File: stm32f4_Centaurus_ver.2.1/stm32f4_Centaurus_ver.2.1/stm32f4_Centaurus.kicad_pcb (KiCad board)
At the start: 2 copper layers, 100 x 79 mm, 215 parts, among them IC1 PIC24FJ64GB004, P1 PICKit3, P10 XA2_12V, P11 CAN0, P12 CAN1, P13 CAN0, P14 CAN1, P15 SERIAL2, P16 SERIAL0, P17 XA2_5V, P18 SWD, P2 SERIAL5_SBDBT, P23 A/D, P24 PWM, P25 A/D_batt, P26 PWM_batt, P27 EMERGENCY_CHECK, P28 I/O_5V, P29 I/O_Variable, P3 ENC0, P30 I/O_5V_batt, P31 I/O_Variable, P4 ENC2, P5 SERIAL1, P6 ENC3, P7 ENC1, P8 SERIAL4, P9 SERIAL3, Q1 FET_P, Q2 FET_P, Q3 FET_P, Q4 NPN, Q5 NPN, Q6 FET_P, Q7 FET_N, SW1 Main_POWER, SW2 SW1, SW3 SW0, SW4 SW2, SW5 SW3, U1 STM32F407VG, U10 LOGO, U12 25LC010A, U13 LOGO, U2 AZ1086H, U3 MCP2221A, U4 BD9G101G, U5 MAX3051, U6 MAX3051, U7 AQM1602_BL, U8 OSTBABS4C2B, U9 LOGO, X1 8MHz

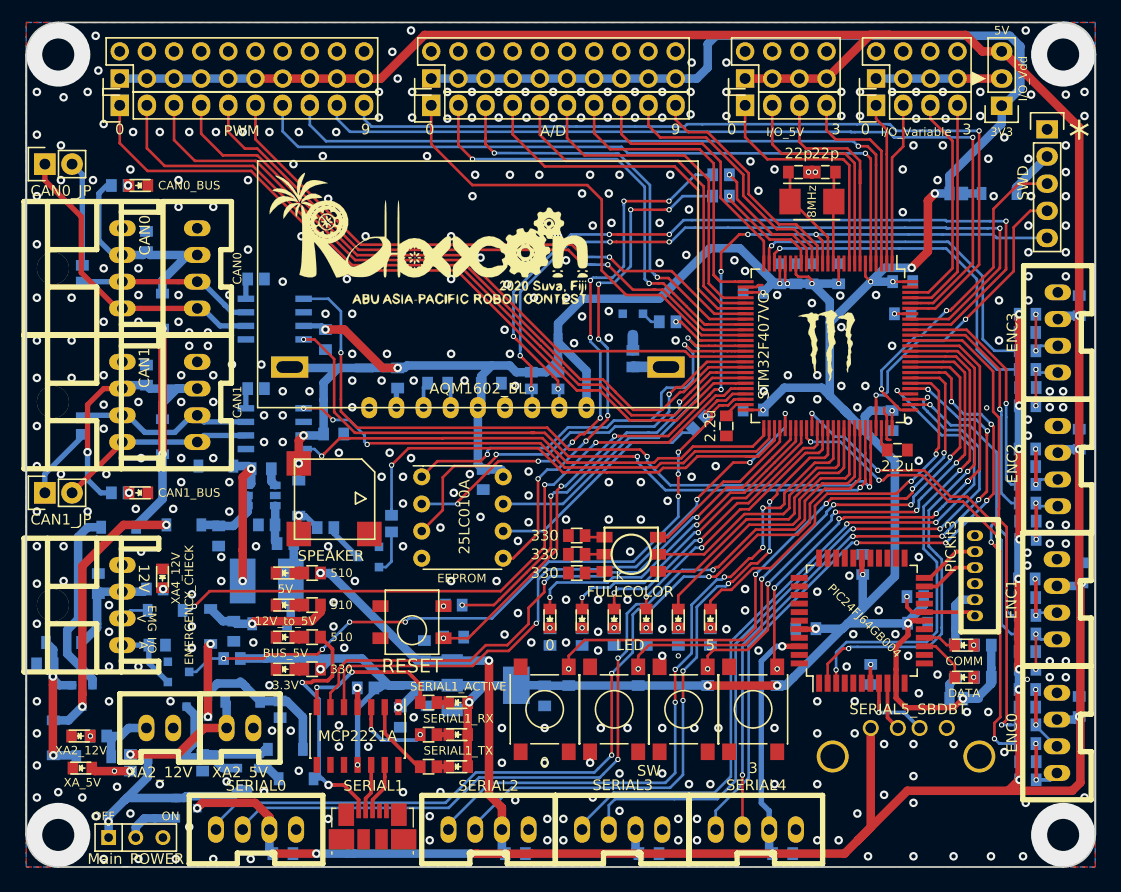
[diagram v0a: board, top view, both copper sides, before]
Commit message: Main typeC化
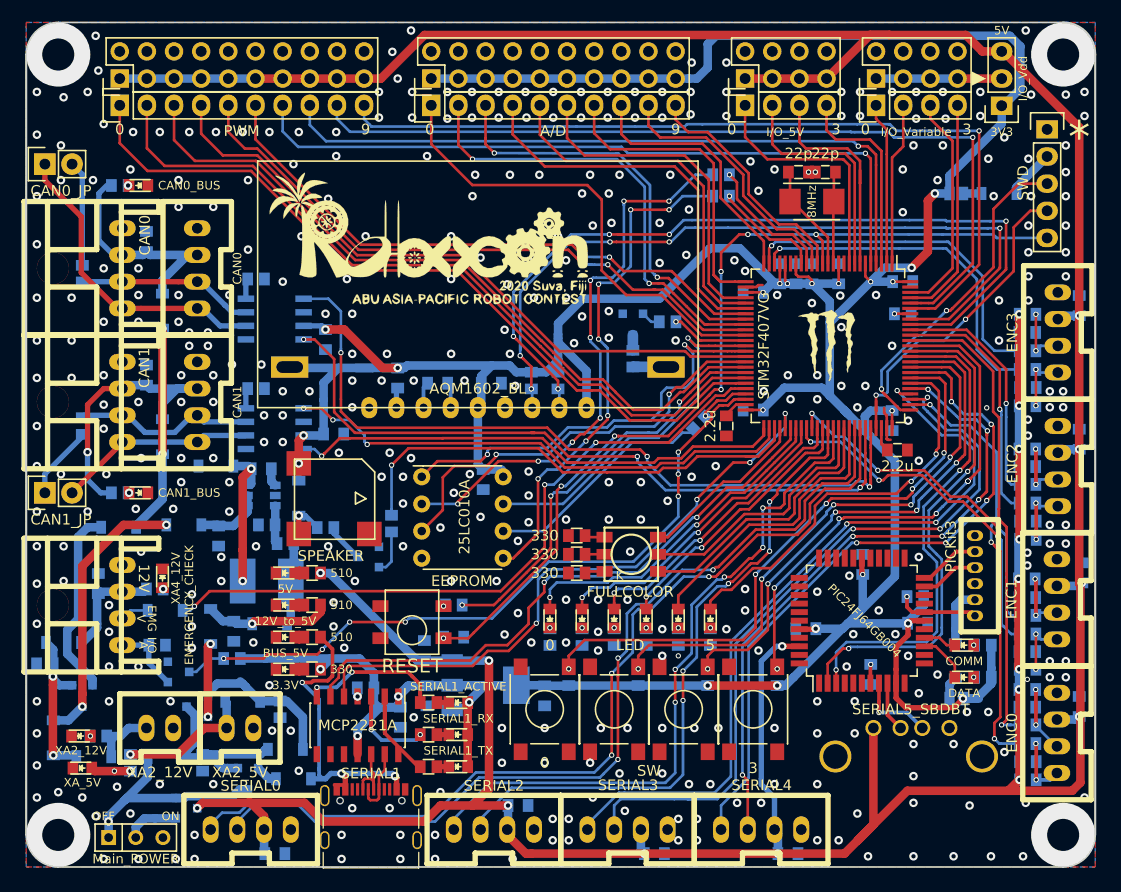
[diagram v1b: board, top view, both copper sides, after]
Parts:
- removed P5: SERIAL1, Mizz_lib:USB_Micro-B_Molex_47346-0001
- added J1: SERIAL1, Connector_USB:USB_C_Receptacle_Palconn_UTC16-G, F.Cu at (85.2, 133.2)
- moved C24 4.51 mm to (99.0, 132.2)
- moved U3 1.00 mm to (84.0, 124.8)
- moved C25 0.75 mm to (76.2, 136.8)
- moved C16 0.50 mm to (124.2, 136.8)
- moved C17 0.50 mm to (111.8, 136.8)
- moved P15 0.50 mm to (93.0, 134.5)
- moved P16 0.50 mm to (70.2, 134.5)
- moved P8 0.50 mm to (118.0, 134.5)
- moved P9 0.50 mm to (105.5, 134.5)
- moved D12 0.25 mm to (78.0, 129.8)
- moved P2 0.25 mm to (132.2, 125.0)
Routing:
- net /BUS_5V: track 23.0 -> 29.3 mm, vias 2 -> 3
- net +5V: track 390.0 -> 394.2 mm, vias 22 -> 19
- net /GP0: track 7.05 -> 10.5 mm
- net /GP1: track 7.39 -> 10.5 mm
- net /USART1_TX: track 84.3 -> 86.6 mm
- net /USART1_RX: track 86.4 -> 88.6 mm
- net /D+_USB: track 4.77 -> 6.32 mm
- net +3V3: track 398.4 -> 397.3 mm
- net Net-(R12-Pad1): track 1.85 -> 0.81 mm
- net /USART3_RX: track 57.5 -> 56.5 mm
- net /USART3_TX: track 59.5 -> 58.5 mm
- net /GP2: track 14.5 -> 13.5 mm
- net /D-_USB: track 4.52 -> 5.39 mm
- net /UART4_TX: track 71.2 -> 70.7 mm
- net /UART4_RX: track 72.2 -> 71.7 mm
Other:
- board text added: "6(type-C,Advanced SBDBT)"
- board text added: "PE10(~WP~)"
- board text added: "PE7(~HOLD~)"
- board text added: "PE8(~CS~)"
- board text added: "SERIAL1"
- board text added: "SPI_MISO"
- board text added: "SPI_MOSI"
- board text added: "SPI_SCk"
- board text removed: "6(microB,Advanced SBDBT)"
